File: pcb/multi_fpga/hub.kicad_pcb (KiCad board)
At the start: 2 copper layers, 167.2 x 167.2 mm, 17 parts, among them J1 PinSocket_2x06_P2.54mm_Vertic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, J2 PinSocket_2x06_P2.54mm_Vertic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, J3 PinSocket_2x06_P2.54mm_Vertic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, J4 PinSocket_2x06_P2.54mm_Vertic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, Y1 TCXO_Can

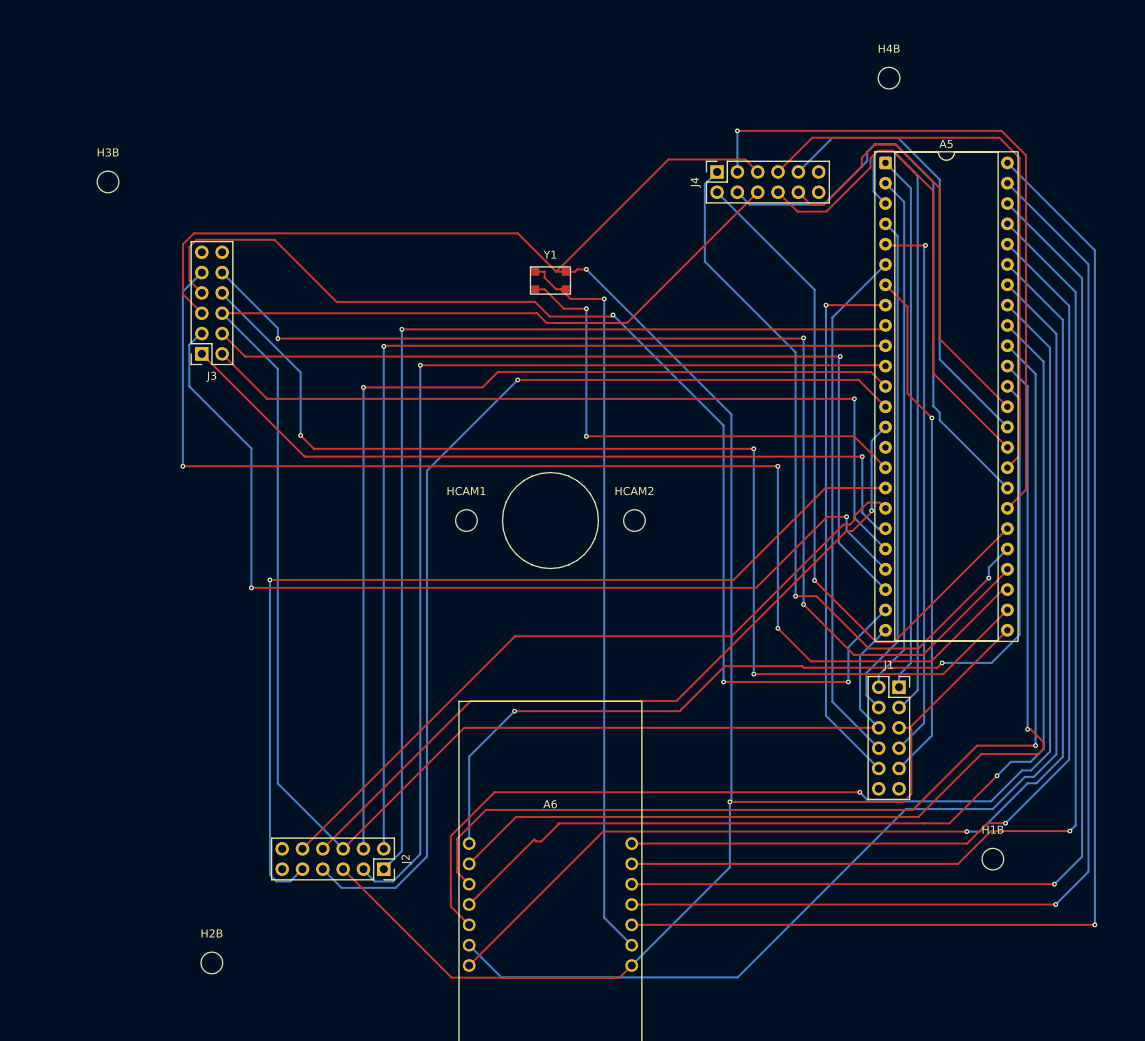
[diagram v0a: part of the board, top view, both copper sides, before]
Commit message: Updated after mic and cap fixes.
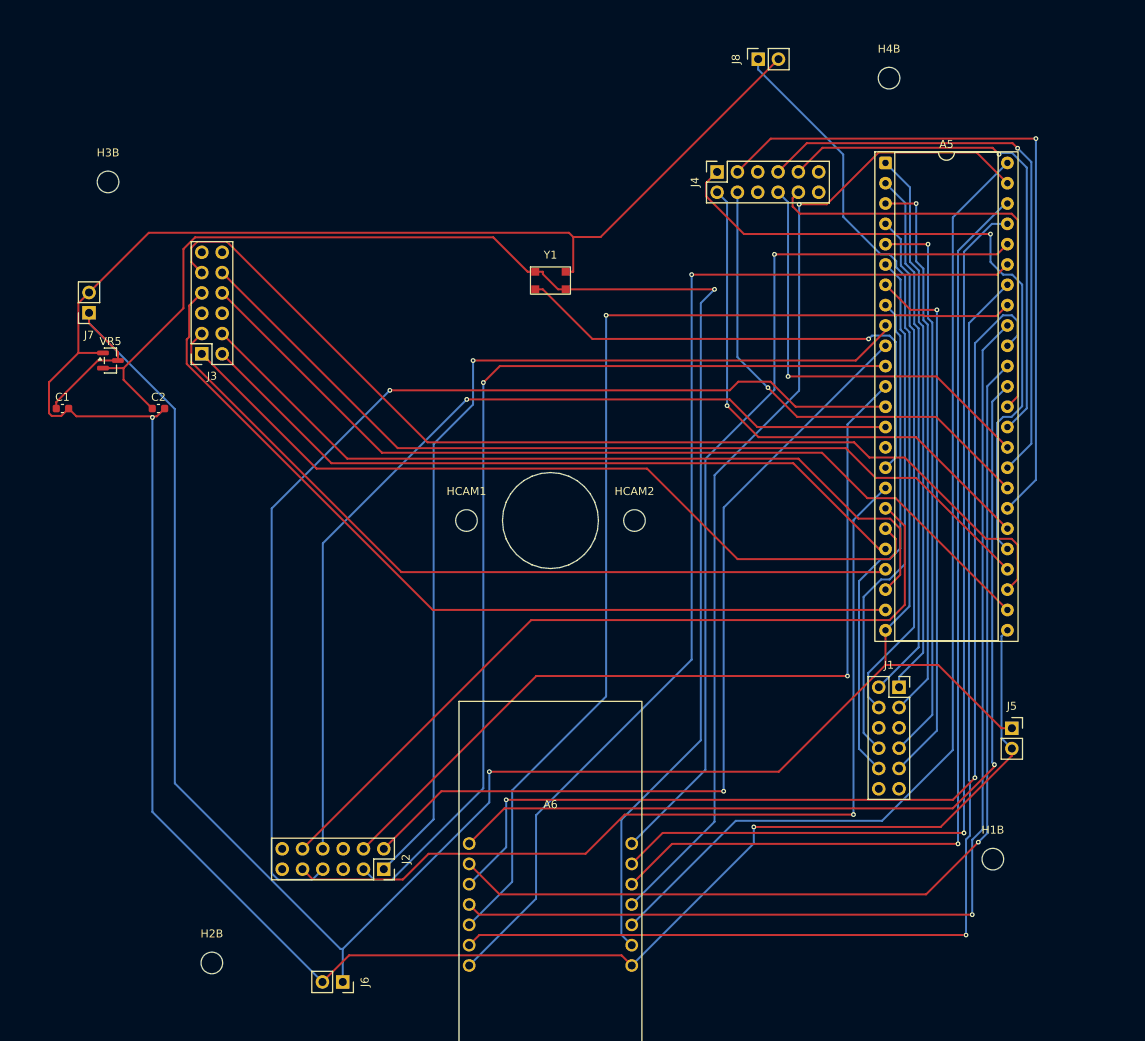
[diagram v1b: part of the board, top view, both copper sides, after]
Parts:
- added C1: C_0603_1608Metric, C_0603_1608Metric, F.Cu at (87.5, 91.0)
- added C2: C_0603_1608Metric, C_0603_1608Metric, F.Cu at (99.5, 91.0)
- added J5: PinSocket_1x02_P2.54mm_Vertical, PinSocket_1x02_P2.54mm_Vertical, F.Cu at (206.2, 131.0)
- added J6: PinSocket_1x02_P2.54mm_Vertical, PinSocket_1x02_P2.54mm_Vertical, F.Cu at (122.5, 162.7)
- added J7: PinSocket_1x02_P2.54mm_Vertical, PinSocket_1x02_P2.54mm_Vertical, F.Cu at (90.8, 79.0)
- added J8: PinSocket_1x02_P2.54mm_Vertical, PinSocket_1x02_P2.54mm_Vertical, F.Cu at (174.5, 47.3)
- added VR5: SOT-23, SOT-23, F.Cu at (93.5, 85.0)
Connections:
- J1 pad 5: GND -> (no net)
- J1 pad 6: +5V -> (no net)
- J2 pad 5: GND -> (no net)
- J2 pad 6: +5V -> (no net)
- J3 pad 5: GND -> (no net)
- J3 pad 6: +5V -> (no net)
- J4 pad 5: GND -> (no net)
- J4 pad 6: +5V -> (no net)
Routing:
- net +3V3: track 93.3 -> 184.3 mm
- net +5V: track 235.1 -> 304.4 mm, vias 0 -> 1
- net GND: track 286.4 -> 336.2 mm
- net USB_WR_N: track 157.7 -> 125.4 mm, vias 1 -> 0
- net SPOKE2_D4: track 141.9 -> 109.7 mm, vias 3 -> 0
- net SPOKE2_CLK: track 142.8 -> 113.5 mm, vias 3 -> 0
- net SPOKE2_D5: track 142.4 -> 114.6 mm, vias 3 -> 0
- net SPOKE2_STROBE: track 153.9 -> 129.1 mm, vias 3 -> 0
- net USB_RD_N: track 149.1 -> 126.5 mm
- net SPOKE2_D2: track 122.4 -> 101.9 mm, vias 2 -> 0
- net SPOKE1_D5: track 97.4 -> 117.4 mm
- net SPOKE3_D1: track 86.7 -> 68.6 mm
- net USB_TXE_N: track 143.2 -> 125.6 mm
- net SPOKE1_D3: track 124.5 -> 107.6 mm
- net USB_D4: track 150.3 -> 134.1 mm
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
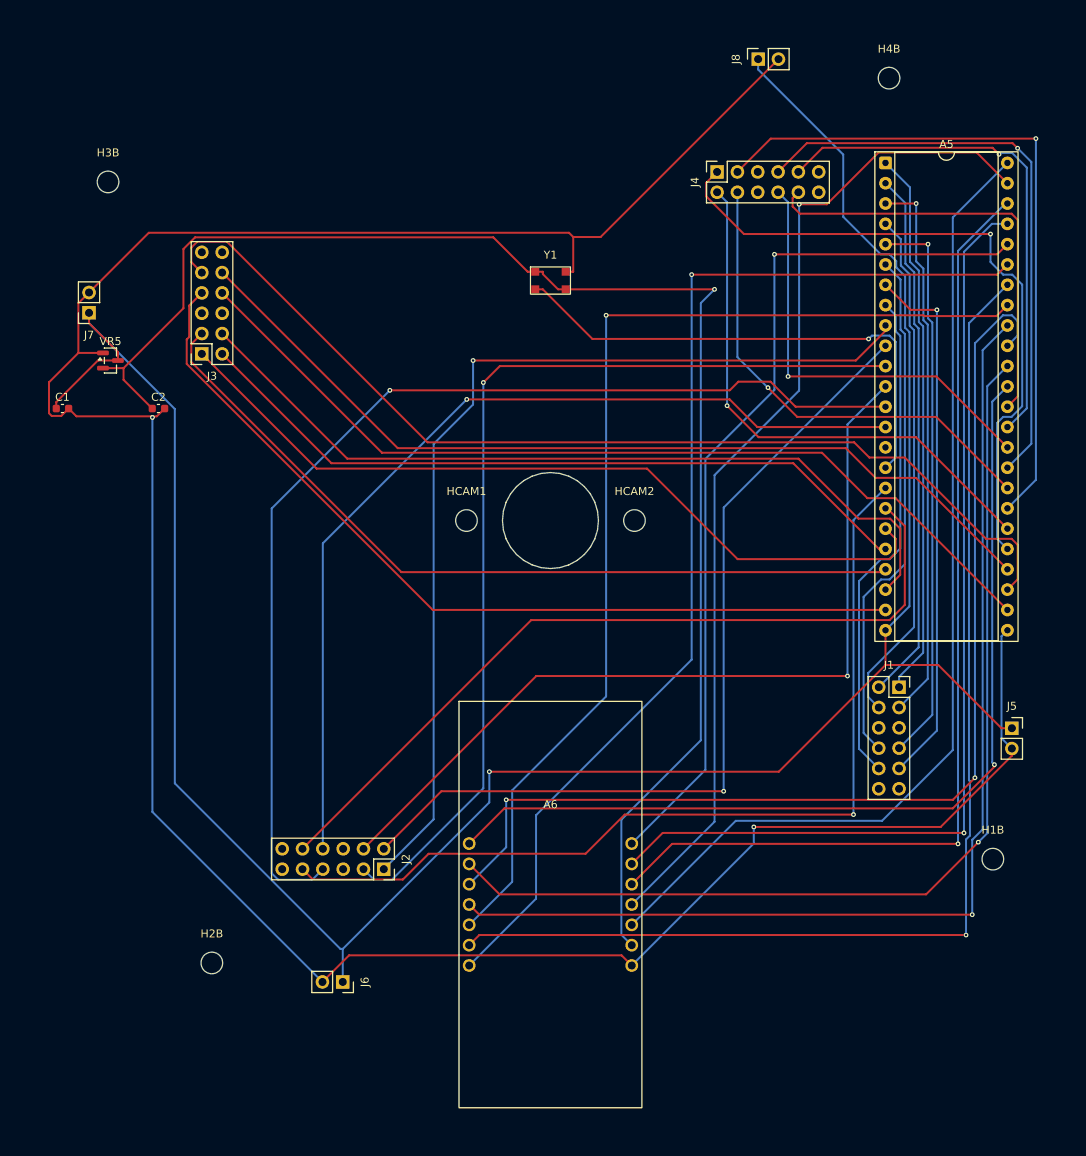
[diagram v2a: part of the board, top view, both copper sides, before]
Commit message: Manually fixed autorouter failures. DRC-clean.
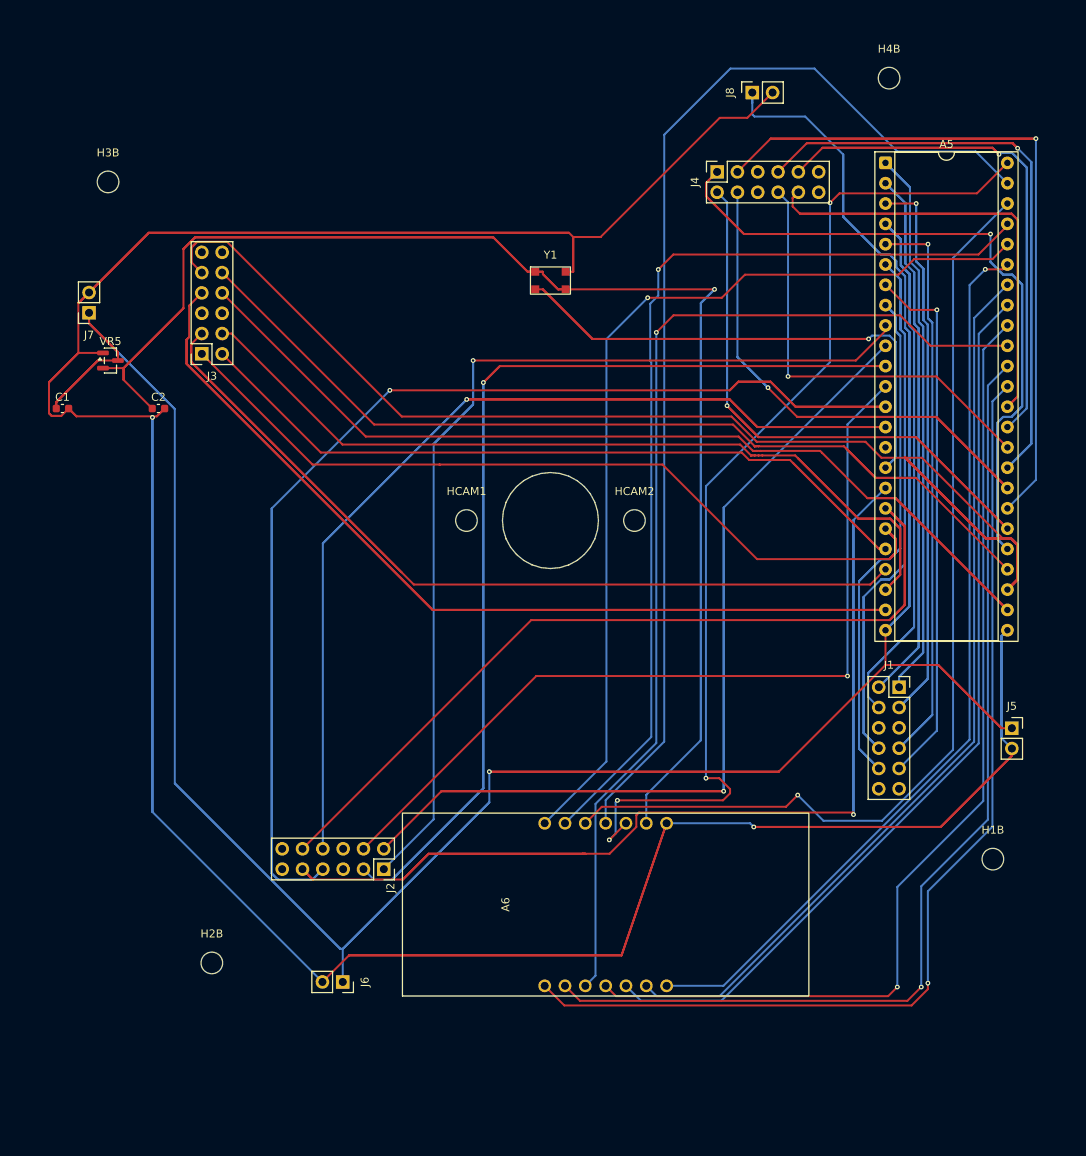
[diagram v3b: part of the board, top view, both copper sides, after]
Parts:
- moved A6 6.90 mm to (155.4, 153.0), turned to 90 degrees
- moved J8 4.24 mm to (173.7, 51.5)
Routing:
- net GND: track 336.2 -> 598.0 mm
- net SPOKE2_D4: track 109.7 -> 316.5 mm
- net +5V: track 304.4 -> 504.3 mm
- net SPOKE2_STROBE: track 129.1 -> 299.3 mm
- net SPOKE0_D3: track 64.9 -> 176.8 mm
- net +3V3: track 184.3 -> 287.3 mm
- net SPOKE1_D4: track 137.5 -> 211.6 mm
- net SPOKE1_D1: track 109.5 -> 180.3 mm
- net SPOKE1_D2: track 122.1 -> 191.9 mm
- net SPOKE0_D0: track 68.7 -> 135.9 mm
- net SPOKE3_D4: track 73.6 -> 139.6 mm
- net SPOKE0_D1: track 66.8 -> 132.0 mm
- net SPOKE0_D2: track 68.9 -> 133.2 mm
- net SPOKE1_STROBE: track 115.2 -> 179.5 mm
- net SPOKE1_D5: track 117.4 -> 180.6 mm
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
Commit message: Moved A6 and manually fixed connections. DRC-clean.
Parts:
- moved A6 1.26 mm to (156.6, 152.6)
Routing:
- net SPOKE1_D1: track 180.3 -> 107.5 mm
- net SPOKE1_STROBE: track 179.5 -> 141.8 mm
- net +5V: track 504.3 -> 468.1 mm
- net USB_WR_N: track 129.5 -> 114.1 mm
- net USB_D6: track 113.2 -> 112.0 mm
- net USB_RXF_N: track 120.3 -> 119.2 mm
- net USB_D7: track 118.8 -> 117.6 mm
- net USB_TXE_N: track 123.5 -> 122.4 mm
- net +3V3: track 287.3 -> 286.4 mm
- net USB_RD_N: track 141.4 -> 140.5 mm
- net USB_D2: track 131.7 -> 130.9 mm
- net GND: track 598.0 -> 598.6 mm

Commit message: Reduced size of the hub board.
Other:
- board size 167.2 x 167.2 mm -> 131.8 x 128.5 mm
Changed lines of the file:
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@@
 	(gr_poly
 		(pts
-			(xy 64.875 21.375) (xy 232.125 21.375) (xy 232.125 188.625) (xy 64.875 188.625)
+			(xy 81.6932 41.20085) (xy 213.484 41.20085) (xy 213.484 169.7412) (xy 81.6932 169.7412)
 		)
 		(stroke

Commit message: Changed to current version of FT232H.
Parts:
- turned A6 to 180 degrees
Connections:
- A6 pad 1: USB_D0 -> (no net)
- A6 pad 10: USB_TXE_N -> USB_D6
- A6 pad 11: USB_RD_N -> USB_D7
- A6 pad 12: USB_WR_N -> (no net)
- A6 pad 13: +3V3 -> (no net)
- A6 pad 14: GND -> (no net)
- A6 pad 2: USB_D1 -> (no net)
- A6 pad 3: USB_D2 -> GND
- A6 pad 4: USB_D3 -> USB_D0
- A6 pad 5: USB_D4 -> USB_D1
- A6 pad 6: USB_D5 -> USB_D2
- A6 pad 7: USB_D6 -> USB_D3
- A6 pad 8: USB_D7 -> USB_D4
- A6 pad 9: USB_RXF_N -> USB_D5
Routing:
- net +3V3: track 286.4 -> 141.4 mm, vias 1 -> 0
- net USB_D0: track 128.9 -> 178.9 mm
- net GND: track 598.6 -> 553.2 mm
- net USB_TXE_N: track 122.4 -> 154.6 mm
- net USB_D6: track 112.0 -> 100.3 mm, vias 1 -> 0
- net USB_RD_N: track 140.5 -> 129.8 mm
- net USB_D7: track 117.6 -> 107.8 mm
- net USB_D5: track 113.4 -> 103.8 mm
- net USB_D4: track 114.2 -> 123.6 mm
- net USB_WR_N: track 114.1 -> 121.2 mm
- net USB_RXF_N: track 119.2 -> 125.8 mm
- net USB_D1: track 127.8 -> 125.4 mm
- net USB_D3: track 125.7 -> 128.0 mm
- net USB_D2: track 130.9 -> 130.0 mm

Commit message: Manually routed. DRC-clean.
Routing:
- net SPOKE2_STROBE: track 299.3 -> 141.1 mm
- net USB_WR_N: track 121.2 -> 266.9 mm, vias 4 -> 2
- net GND: track 553.2 -> 433.7 mm, vias 2 -> 1
- net +5V: track 468.1 -> 397.6 mm
- net SPOKE1_D5: track 180.6 -> 126.6 mm
- net SPOKE1_D2: track 191.9 -> 138.4 mm
- net SPOKE1_D4: track 211.6 -> 162.2 mm
- net TCXO_CLK: track 109.5 -> 75.0 mm
- net USB_D7: track 107.8 -> 139.8 mm
- net SPOKE3_D2: track 119.9 -> 88.6 mm
- net SPOKE3_D1: track 115.8 -> 85.4 mm
- net USB_D2: track 130.0 -> 159.6 mm
- net USB_D6: track 100.3 -> 129.6 mm, vias 0 -> 1
- net SPOKE1_STROBE: track 141.8 -> 114.9 mm
- net SPOKE3_D4: track 139.6 -> 114.1 mm
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- removed copper zone on F.Cu, net GND

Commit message: Manual routing changes.
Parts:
- moved HPI1 158.0 mm to (119.0, 78.5)
- moved HPI2 158.0 mm to (177.0, 78.5)
- moved HPI3 158.0 mm to (119.0, 127.5)
- moved HPI4 158.0 mm to (177.0, 127.5)
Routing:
- net USB_WR_N: track 266.9 -> 131.4 mm
- net SPOKE2_D4: track 316.5 -> 228.3 mm
- net USB_D0: track 159.2 -> 103.7 mm
- net +3V3: track 141.4 -> 95.1 mm
- net SPOKE2_D2: track 143.1 -> 106.0 mm
- net SPOKE3_STROBE: track 97.4 -> 67.0 mm
- net USB_RD_N: track 145.2 -> 132.2 mm, vias 0 -> 2
- net +5V: track 397.6 -> 386.5 mm
- net SPOKE2_STROBE: track 141.1 -> 134.1 mm
- net SPOKE1_STROBE: track 114.9 -> 119.9 mm
- net SPOKE1_D1: track 107.5 -> 112.2 mm
- net GND: track 433.7 -> 430.6 mm
- net SPOKE3_D4: track 114.1 -> 116.8 mm
- net SPOKE3_D2: track 88.6 -> 90.7 mm
- net USB_RXF_N: track 124.4 -> 122.5 mm
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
